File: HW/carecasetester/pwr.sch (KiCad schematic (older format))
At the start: 5 parts, among them J5 12V_Psu, U2 L7805

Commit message: cc-tester v0.1 gerber filser genereret og 1. print bestilles
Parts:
- C1, C2, C3: footprint (none) -> Capacitor_SMD:C_0603_1608Metric_Pad1.05x0.95mm_HandSolder
- J5: footprint (none) -> athir:Friwo_Texas_2-pin_Plug(1321609)
- U2: footprint (none) -> Package_TO_SOT_THT:TO-220-3_Vertical
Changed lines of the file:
@@
 $Descr A4 11693 8268
 encoding utf-8
-Sheet 5 5
+Sheet 5 6
 Title ""
 Date ""
@@
 F 0 "J5" V 3762 1319 50  0000 L CNN
 F 1 "12V_Psu" V 3853 1319 50  0000 L CNN
-F 2 "" H 3700 1275 50  0001 C CNN
+F 2 "athir:Friwo_Texas_2-pin_Plug(1321609)" H 3700 1275 50  0001 C CNN
 F 3 "~" H 3700 1275 50  0001 C CNN
 	1    3700 1275
@@
 F 0 "U2" H 6350 2067 50  0000 C CNN
 F 1 "L7805" H 6350 1976 50  0000 C CNN
-F 2 "" H 6375 1675 50  0001 L CIN
+F 2 "Package_TO_SOT_THT:TO-220-3_Vertical" H 6375 1675 50  0001 L CIN
 F 3 "http://www.st.com/content/ccc/resource/technical/document/datasheet/41/4f/b3/b0/12/d4/47/88/CD00000444.pdf/files/CD00000444.pdf/jcr:content/translations/en.CD00000444.pdf" H 6350 1775 50  0001 C CNN
 	1    6350 1825
@@
 F 0 "C3" V 6850 1800 50  0000 L CNN
 F 1 "100µf" V 7000 1800 50  0000 L CNN
-F 2 "" H 6900 1925 50  0001 C CNN
+F 2 "Capacitor_SMD:C_0603_1608Metric_Pad1.05x0.95mm_HandSolder" H 6900 1925 50  0001 C CNN
 F 3 "~" H 6900 1925 50  0001 C CNN
 	1    6900 1925
@@
 F 0 "C2" V 6600 1800 50  0000 L CNN
 F 1 "100nf" V 6775 1800 50  0000 L CNN
-F 2 "" H 6675 1925 50  0001 C CNN
+F 2 "Capacitor_SMD:C_0603_1608Metric_Pad1.05x0.95mm_HandSolder" H 6675 1925 50  0001 C CNN
 F 3 "~" H 6675 1925 50  0001 C CNN
 	1    6675 1925
@@
 F 0 "C1" V 5875 1775 50  0000 L CNN
 F 1 "100µf" V 6050 1775 50  0000 L CNN
-F 2 "" H 5950 1925 50  0001 C CNN
+F 2 "Capacitor_SMD:C_0603_1608Metric_Pad1.05x0.95mm_HandSolder" H 5950 1925 50  0001 C CNN
 F 3 "~" H 5950 1925 50  0001 C CNN
 	1    5950 1925

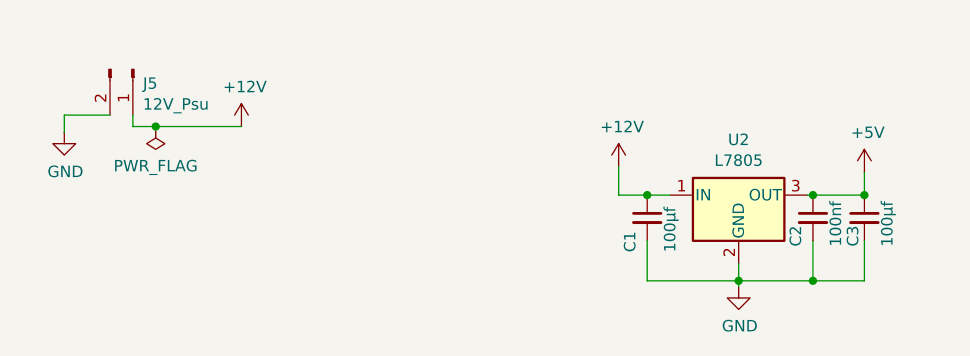
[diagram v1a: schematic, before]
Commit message: First try to fit schematic to pcb (not imported footprints to pcb yet)
Schematic: All known components has gotten an updated footprint
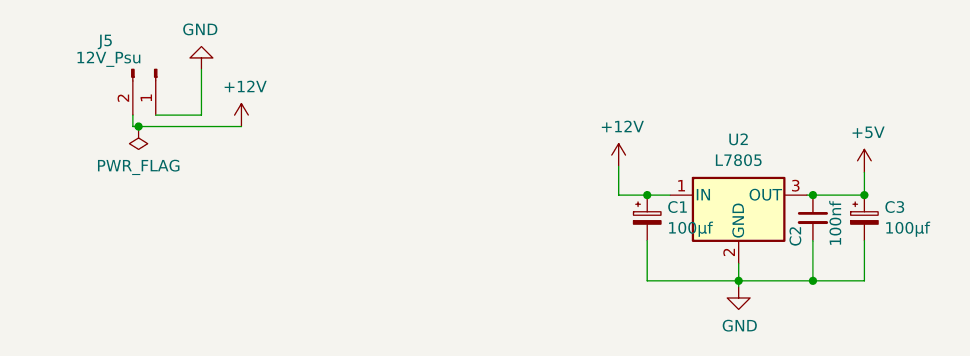
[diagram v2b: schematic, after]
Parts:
- removed C1, C3: 100µf, Capacitor_SMD:C_0603_1608Metric_Pad1.05x0.95mm_HandSolder, symbol Device:C_Small
- added C1, C3: 100µf, Capacitor_SMD:CP_Elec_6.3x5.4, symbol Device:CP_Small
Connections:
- net +12V: now also J5.2 (Pin_2), C1.1; no longer J5.1 (Pin_1)
- net +5V: now also C3.1
- net GND: now also J5.1 (Pin_1), C1.2, C3.2; no longer J5.2 (Pin_2)
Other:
- moved on the sheet: J5
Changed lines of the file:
@@
 L Connector:Conn_01x02_Male J5
 U 1 1 5E43E40C
-P 3700 1275
-F 0 "J5" V 3762 1319 50  0000 L CNN
-F 1 "12V_Psu" V 3853 1319 50  0000 L CNN
-F 2 "athir:Friwo_Texas_2-pin_Plug(1321609)" H 3700 1275 50  0001 C CNN
-F 3 "~" H 3700 1275 50  0001 C CNN
-	1    3700 1275
+P 3800 1275
+F 0 "J5" V 3675 1025 50  0000 L CNN
+F 1 "12V_Psu" V 3750 925 50  0000 L CNN
+F 2 "athir:Friwo_Texas_2-pin_Plug(1321609)" H 3800 1275 50  0001 C CNN
+F 3 "~" H 3800 1275 50  0001 C CNN
+	1    3800 1275
 	0    1    1    0
 $EndComp
@@
 L power:GND #PWR0107
 U 1 1 5E43EAF3
-P 3400 1550
-F 0 "#PWR0107" H 3400 1300 50  0001 C CNN
-F 1 "GND" H 3405 1377 50  0000 C CNN
-F 2 "" H 3400 1550 50  0001 C CNN
-F 3 "" H 3400 1550 50  0001 C CNN
-	1    3400 1550
-	1    0    0    -1
+P 4000 1275
+F 0 "#PWR0107" H 4000 1025 50  0001 C CNN
+F 1 "GND" H 4005 1102 50  0000 C CNN
+F 2 "" H 4000 1275 50  0001 C CNN
+F 3 "" H 4000 1275 50  0001 C CNN
+	1    4000 1275
+	-1   0    0    1
 $EndComp
-Wire Wire Line
-	3400 1550 3400 1475
-Wire Wire Line
-	3400 1475 3600 1475
 $Comp
 L Regulator_Linear:L7805 U2
@@
 	3700 1475 3700 1525
 Wire Wire Line
-	3700 1525 3800 1525
+	3700 1525 3725 1525
 $Comp
 L power:+12V #PWR0114
@@
 Wire Wire Line
 	5825 1700 5825 1825
-Wire Wire Line
-	5825 1825 5950 1825
 $Comp
 L power:GND #PWR0115
@@
 	6900 1825 6900 1725
 $Comp
-L Device:C_Small C3
-U 1 1 5E4433EB
-P 6900 1925
-F 0 "C3" V 6850 1800 50  0000 L CNN
-F 1 "100µf" V 7000 1800 50  0000 L CNN
-F 2 "Capacitor_SMD:C_0603_1608Metric_Pad1.05x0.95mm_HandSolder" H 6900 1925 50  0001 C CNN
-F 3 "~" H 6900 1925 50  0001 C CNN
-	1    6900 1925
-	1    0    0    -1
-$EndComp
-Connection ~ 6900 1825
-$Comp
 L Device:C_Small C2
 U 1 1 5E443BBB
@@
 Wire Wire Line
 	6675 1825 6900 1825
-$Comp
-L Device:C_Small C1
-U 1 1 5E443F52
-P 5950 1925
-F 0 "C1" V 5875 1775 50  0000 L CNN
-F 1 "100µf" V 6050 1775 50  0000 L CNN
-F 2 "Capacitor_SMD:C_0603_1608Metric_Pad1.05x0.95mm_HandSolder" H 5950 1925 50  0001 C CNN
-F 3 "~" H 5950 1925 50  0001 C CNN
-	1    5950 1925
-	1    0    0    -1
-$EndComp
-Connection ~ 5950 1825
-Wire Wire Line
-	5950 1825 6050 1825
 Wire Wire Line
 	5950 2025 5950 2200
@@
 L power:PWR_FLAG #FLG0102
 U 1 1 5E4462F1
-P 3800 1525
-F 0 "#FLG0102" H 3800 1600 50  0001 C CNN
-F 1 "PWR_FLAG" H 3800 1698 50  0000 C CNN
-F 2 "" H 3800 1525 50  0001 C CNN
-F 3 "~" H 3800 1525 50  0001 C CNN
-	1    3800 1525
+P 3725 1525
+F 0 "#FLG0102" H 3725 1600 50  0001 C CNN
+F 1 "PWR_FLAG" H 3725 1698 50  0000 C CNN
+F 2 "" H 3725 1525 50  0001 C CNN
+F 3 "~" H 3725 1525 50  0001 C CNN
+	1    3725 1525
 	-1   0    0    1
 $EndComp
-Connection ~ 3800 1525
 Wire Wire Line
-	3800 1525 4175 1525
+	4000 1275 4000 1475
+Wire Wire Line
+	4000 1475 3800 1475
+$Comp
+L Device:CP_Small C1
+U 1 1 5E8637F9
+P 5950 1925
+F 0 "C1" H 6038 1971 50  0000 L CNN
+F 1 "100µf" H 6038 1880 50  0000 L CNN
+F 2 "Capacitor_SMD:CP_Elec_6.3x5.4" H 5950 1925 50  0001 C CNN
+F 3 "~" H 5950 1925 50  0001 C CNN
+	1    5950 1925
+	1    0    0    -1
+$EndComp
+Wire Wire Line
+	5825 1825 5950 1825
+Connection ~ 5950 1825
+Wire Wire Line
+	5950 1825 6050 1825
+$Comp
+L Device:CP_Small C3
+U 1 1 5E866000
+P 6900 1925
+F 0 "C3" H 6988 1971 50  0000 L CNN
+F 1 "100µf" H 6988 1880 50  0000 L CNN
+F 2 "Capacitor_SMD:CP_Elec_6.3x5.4" H 6900 1925 50  0001 C CNN
+F 3 "~" H 6900 1925 50  0001 C CNN
+	1    6900 1925
+	1    0    0    -1
+$EndComp
+Connection ~ 6900 1825
+Connection ~ 3725 1525
+Wire Wire Line
+	3725 1525 4175 1525
 $EndSCHEMATC

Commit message: PCB and Schematic are synced and gerbers can be made
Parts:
- U2: footprint Package_TO_SOT_THT:TO-220-3_Vertical -> Package_TO_SOT_THT:TO-220-3_Horizontal_TabDown
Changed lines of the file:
@@
 F 0 "U2" H 6350 2067 50  0000 C CNN
 F 1 "L7805" H 6350 1976 50  0000 C CNN
-F 2 "Package_TO_SOT_THT:TO-220-3_Vertical" H 6375 1675 50  0001 L CIN
+F 2 "Package_TO_SOT_THT:TO-220-3_Horizontal_TabDown" H 6375 1675 50  0001 L CIN
 F 3 "http://www.st.com/content/ccc/resource/technical/document/datasheet/41/4f/b3/b0/12/d4/47/88/CD00000444.pdf/files/CD00000444.pdf/jcr:content/translations/en.CD00000444.pdf" H 6350 1775 50  0001 C CNN
 	1    6350 1825

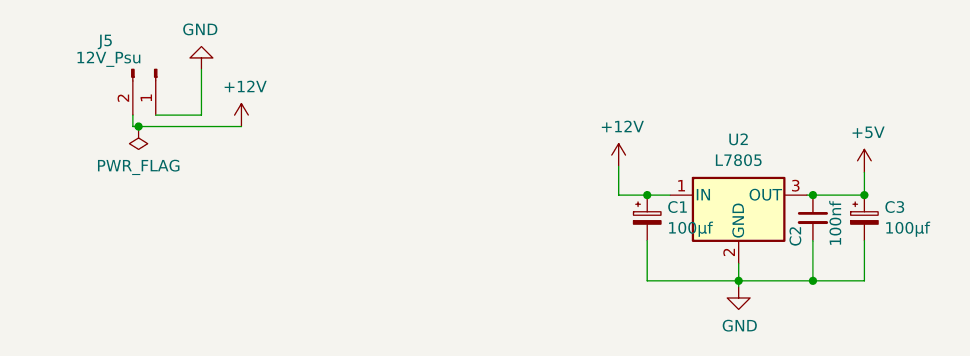
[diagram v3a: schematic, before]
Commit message: Gerbers and drillfiles made and ready to order
edge cuts file renamed to GML instaid of GM1
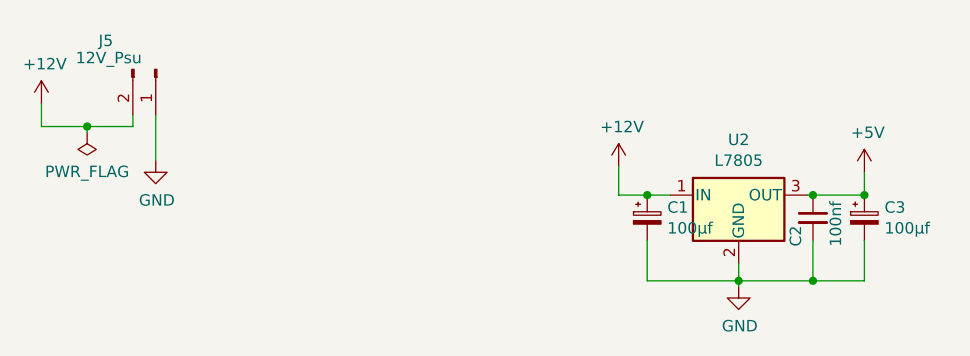
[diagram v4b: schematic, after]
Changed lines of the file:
@@
 L power:GND #PWR0107
 U 1 1 5E43EAF3
-P 4000 1275
-F 0 "#PWR0107" H 4000 1025 50  0001 C CNN
-F 1 "GND" H 4005 1102 50  0000 C CNN
-F 2 "" H 4000 1275 50  0001 C CNN
-F 3 "" H 4000 1275 50  0001 C CNN
-	1    4000 1275
-	-1   0    0    1
+P 3800 1675
+F 0 "#PWR0107" H 3800 1425 50  0001 C CNN
+F 1 "GND" H 3805 1502 50  0000 C CNN
+F 2 "" H 3800 1675 50  0001 C CNN
+F 3 "" H 3800 1675 50  0001 C CNN
+	1    3800 1675
+	1    0    0    -1
 $EndComp
 $Comp
@@
 L power:+12V #PWR0113
 U 1 1 5E4412C4
-P 4175 1525
-F 0 "#PWR0113" H 4175 1375 50  0001 C CNN
-F 1 "+12V" H 4190 1698 50  0000 C CNN
-F 2 "" H 4175 1525 50  0001 C CNN
-F 3 "" H 4175 1525 50  0001 C CNN
-	1    4175 1525
+P 3300 1425
+F 0 "#PWR0113" H 3300 1275 50  0001 C CNN
+F 1 "+12V" H 3315 1598 50  0000 C CNN
+F 2 "" H 3300 1425 50  0001 C CNN
+F 3 "" H 3300 1425 50  0001 C CNN
+	1    3300 1425
 	1    0    0    -1
 $EndComp
 Wire Wire Line
 	3700 1475 3700 1525
-Wire Wire Line
-	3700 1525 3725 1525
 $Comp
 L power:+12V #PWR0114
@@
 L power:PWR_FLAG #FLG0102
 U 1 1 5E4462F1
-P 3725 1525
-F 0 "#FLG0102" H 3725 1600 50  0001 C CNN
-F 1 "PWR_FLAG" H 3725 1698 50  0000 C CNN
-F 2 "" H 3725 1525 50  0001 C CNN
-F 3 "~" H 3725 1525 50  0001 C CNN
-	1    3725 1525
+P 3500 1550
+F 0 "#FLG0102" H 3500 1625 50  0001 C CNN
+F 1 "PWR_FLAG" H 3500 1723 50  0000 C CNN
+F 2 "" H 3500 1550 50  0001 C CNN
+F 3 "~" H 3500 1550 50  0001 C CNN
+	1    3500 1550
 	-1   0    0    1
 $EndComp
-Wire Wire Line
-	4000 1275 4000 1475
-Wire Wire Line
-	4000 1475 3800 1475
 $Comp
 L Device:CP_Small C1
@@
 $EndComp
 Connection ~ 6900 1825
-Connection ~ 3725 1525
 Wire Wire Line
-	3725 1525 4175 1525
+	3700 1525 3500 1525
+Wire Wire Line
+	3500 1525 3500 1550
+Wire Wire Line
+	3500 1525 3300 1525
+Wire Wire Line
+	3300 1525 3300 1425
+Connection ~ 3500 1525
+Wire Wire Line
+	3800 1675 3800 1475
 $EndSCHEMATC
